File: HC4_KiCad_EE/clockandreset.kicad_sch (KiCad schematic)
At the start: 18 parts, among them IC15 74HC14, SW2 SW_Push, SW3 SW_Push, SW4 FreqSel, SW5 SW_SPDT

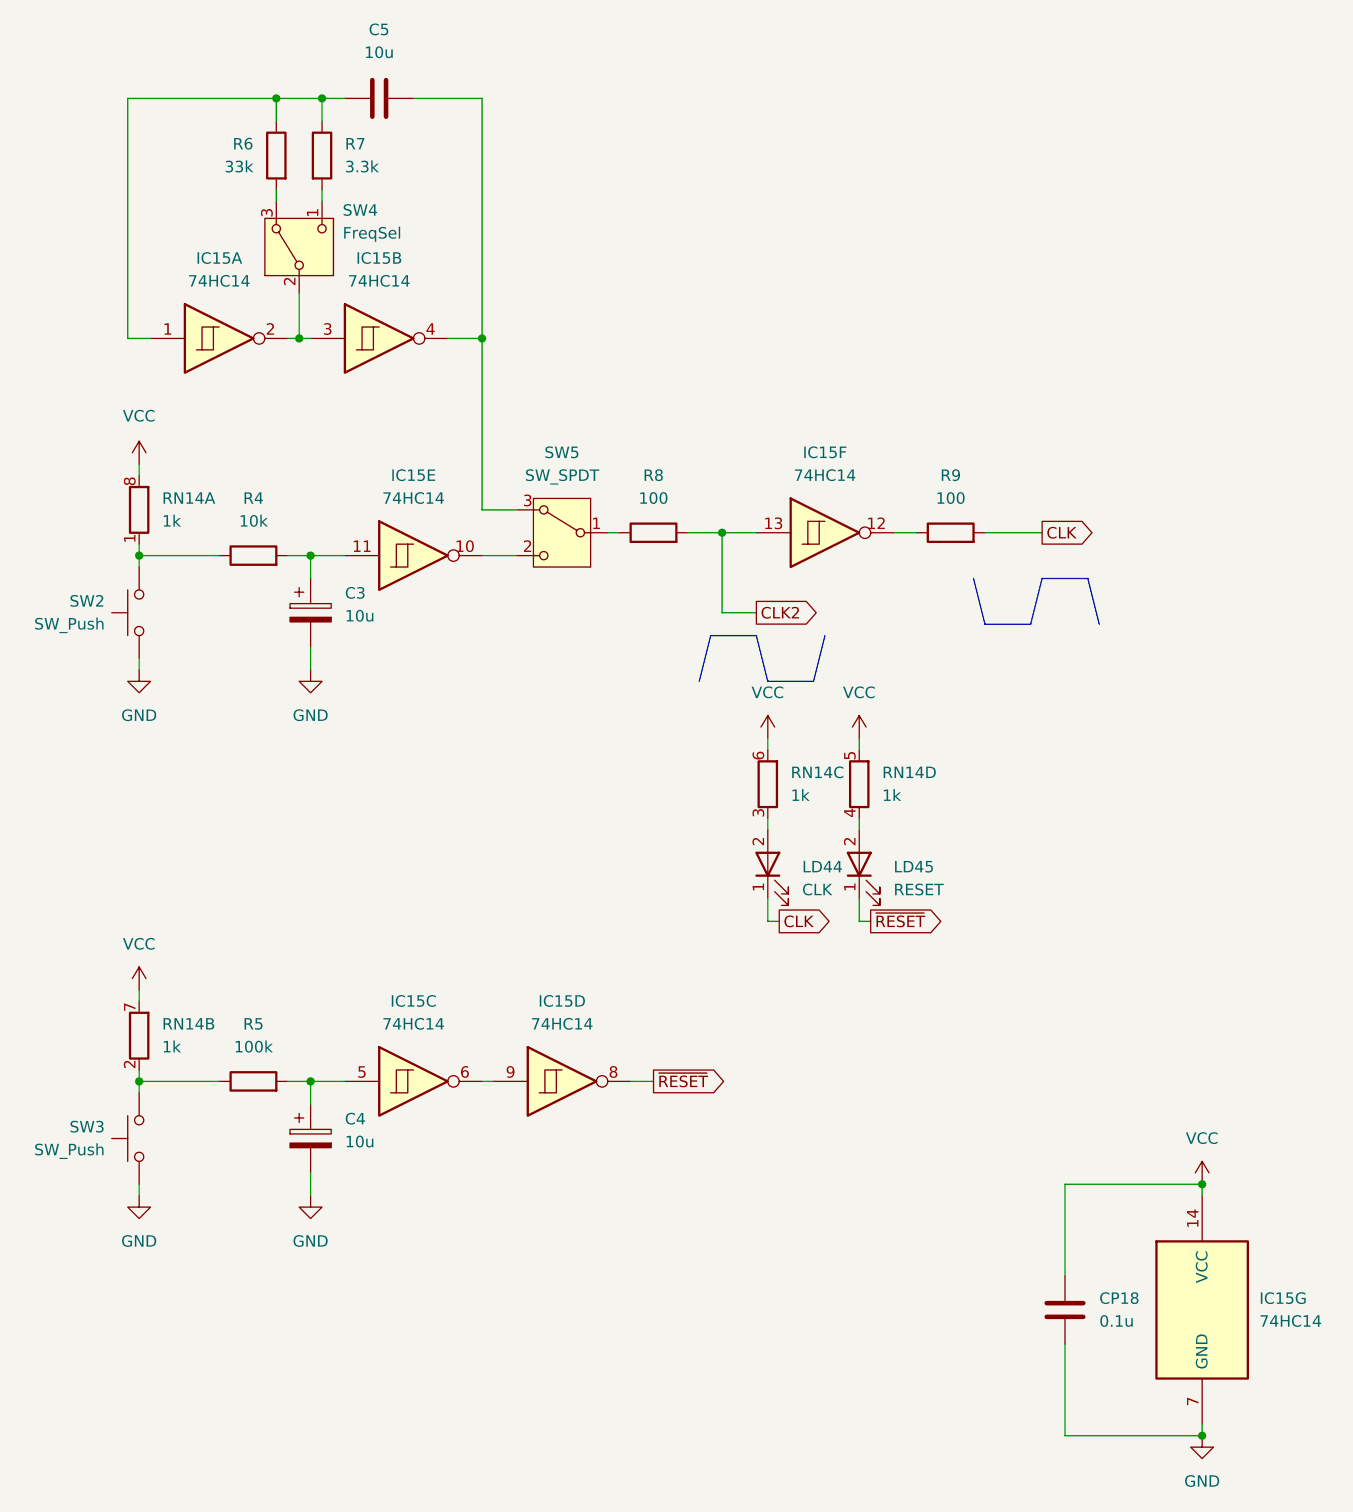
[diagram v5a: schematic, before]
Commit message: 配線進捗、7474を使った変な回路
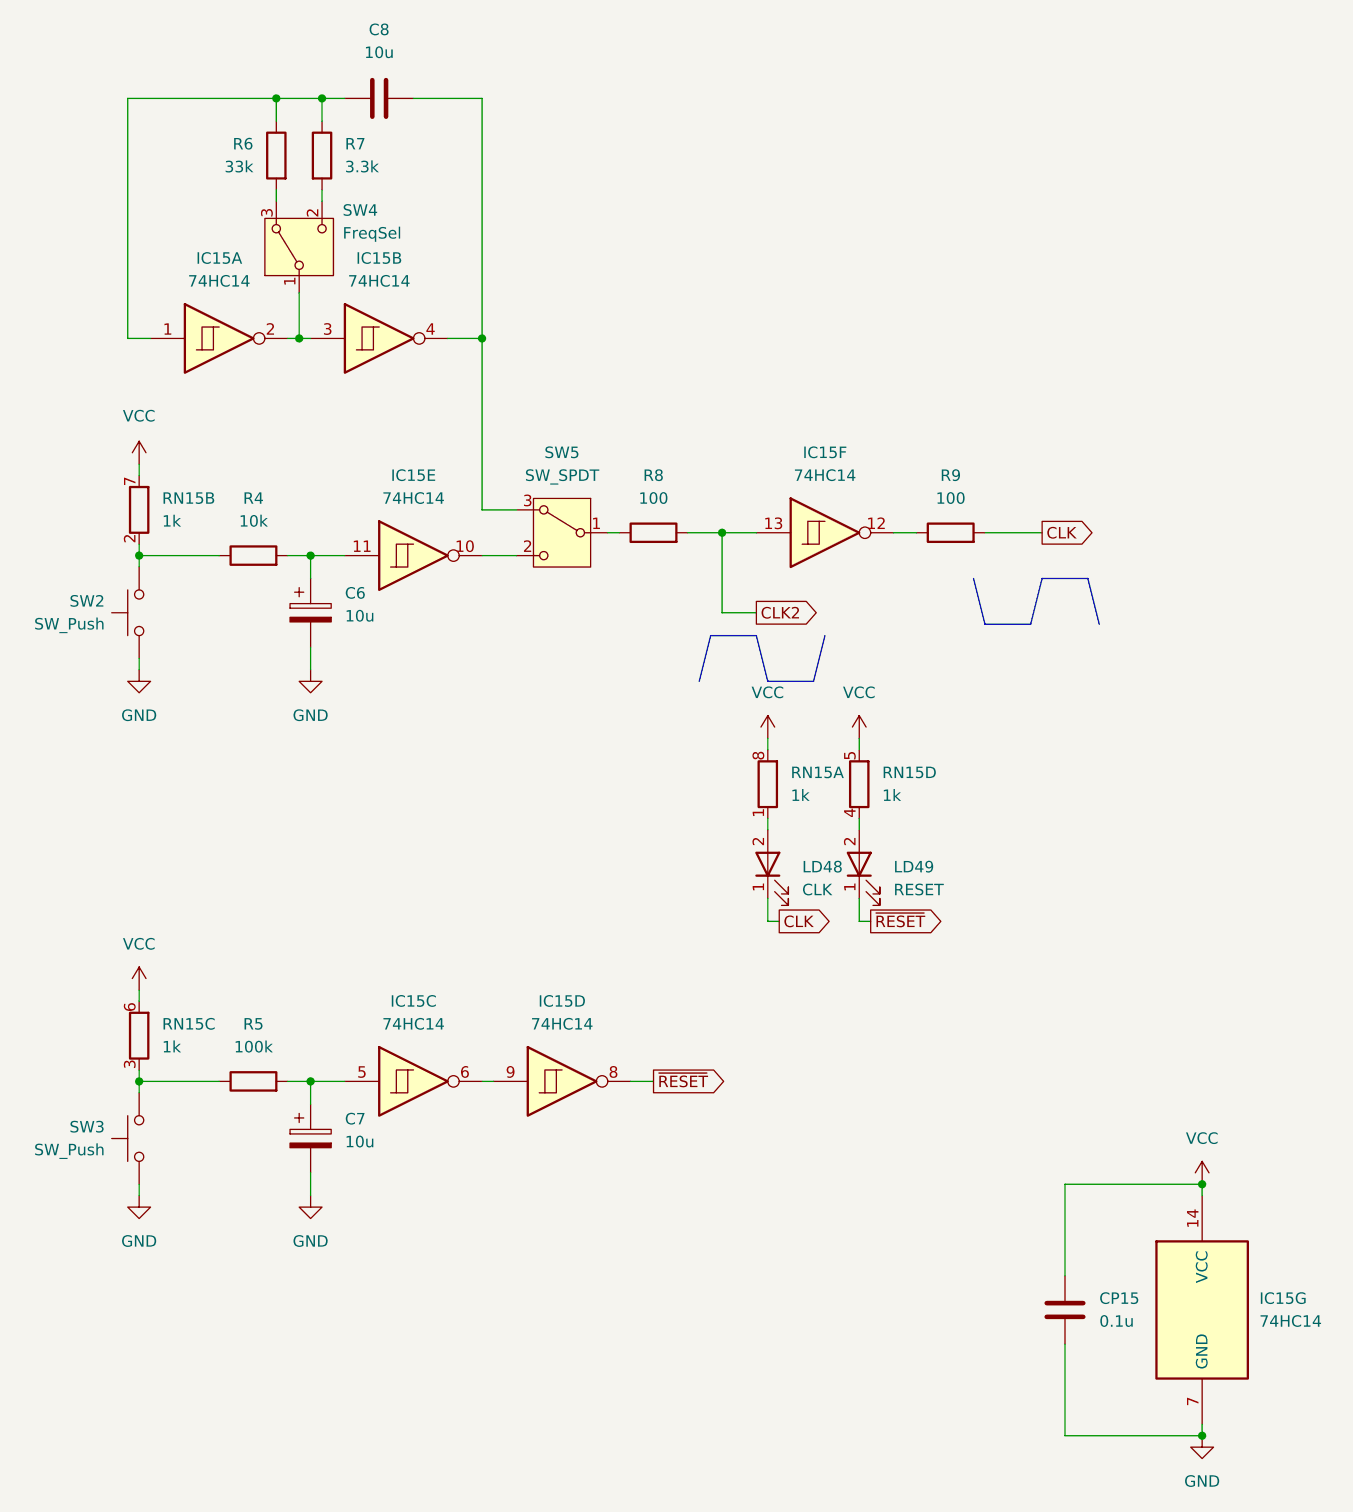
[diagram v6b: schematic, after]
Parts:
- SW4: symbol Switch:SW_SPDT_321 -> Switch:SW_SPDT_312
- renumbered C3 to C6, C4 to C7, C5 to C8, CP18 to CP15, LD44 to LD48, LD45 to LD49, RN14 to RN15
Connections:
- net at R4.1, SW2.2: now also RN15.2 (R2.1); no longer RN15.1 (R1.1)
- net at R5.1, SW3.2: now also RN15.3 (R3.1); no longer RN15.2 (R2.1)
- net at SW4.1 (B): now also IC15.2, IC15.3; no longer R7.2
- net at LD48.2: now also RN15.1 (R1.1); no longer RN15.3 (R3.1)
- new net: R7.2, SW4.2 (C)
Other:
- moved on the sheet: RN15A, RN15B, RN15C
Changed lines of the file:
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@@
 		(dnp no)
 		(fields_autoplaced yes)
-		(property "Reference" "RN14"
+		(property "Reference" "RN15"
 			(at 120.65 116.8399 0)
 			(effects
@@
 			(project ""
 				(path "/33731ded-38c0-4297-bdd8-92b082f46ff8/3d67359d-c55c-4207-8a6b-ff7c83e276f6"
-					(reference "RN14")
+					(reference "RN15")
 					(unit 4)
 				)
@@
 	(symbol
 		(lib_id "Device:R_Pack04_Split")
-		(at 38.1 146.05 0)
+		(at 38.1 87.63 0)
 		(unit 2)
 		(exclude_from_sim no)
@@
 		(dnp no)
 		(fields_autoplaced yes)
-		(property "Reference" "RN14"
-			(at 40.64 144.7799 0)
+		(property "Reference" "RN15"
+			(at 40.64 86.3599 0)
 			(effects
 				(font
@@
 		)
 		(property "Value" "1k"
-			(at 40.64 147.3199 0)
+			(at 40.64 88.8999 0)
 			(effects
 				(font
@@
 		)
 		(property "Footprint" "Resistor_SMD:R_Array_Convex_4x0603"
-			(at 36.068 146.05 90)
+			(at 36.068 87.63 90)
 			(effects
 				(font
@@
 		)
 		(property "Datasheet" "~"
-			(at 38.1 146.05 0)
+			(at 38.1 87.63 0)
 			(effects
 				(font
@@
 		)
 		(property "Description" "4 resistor network, parallel topology, split"
-			(at 38.1 146.05 0)
+			(at 38.1 87.63 0)
 			(effects
 				(font
@@
 			(project ""
 				(path "/33731ded-38c0-4297-bdd8-92b082f46ff8/3d67359d-c55c-4207-8a6b-ff7c83e276f6"
-					(reference "RN14")
+					(reference "RN15")
 					(unit 2)
 				)
@@
 		(dnp no)
 		(fields_autoplaced yes)
-		(property "Reference" "#PWR073"
+		(property "Reference" "#PWR072"
 			(at 118.11 116.84 0)
 			(effects
@@
 			(project ""
 				(path "/33731ded-38c0-4297-bdd8-92b082f46ff8/3d67359d-c55c-4207-8a6b-ff7c83e276f6"
-					(reference "#PWR073")
+					(reference "#PWR072")
 					(unit 1)
 				)
@@
 		(dnp no)
 		(fields_autoplaced yes)
-		(property "Reference" "C5"
+		(property "Reference" "C8"
 			(at 64.77 34.29 90)
 			(effects
@@
 			(project ""
 				(path "/33731ded-38c0-4297-bdd8-92b082f46ff8/3d67359d-c55c-4207-8a6b-ff7c83e276f6"
-					(reference "C5")
+					(reference "C8")
 					(unit 1)
 				)
@@
 		(dnp no)
 		(fields_autoplaced yes)
-		(property "Reference" "#PWR067"
+		(property "Reference" "#PWR066"
 			(at 38.1 111.76 0)
 			(effects
@@
 			(project "HC4_KiCad"
 				(path "/33731ded-38c0-4297-bdd8-92b082f46ff8/3d67359d-c55c-4207-8a6b-ff7c83e276f6"
-					(reference "#PWR067")
-					(unit 1)
-				)
-			)
-		)
-	)
-	(symbol
-		(lib_id "Switch:SW_SPDT_321")
+					(reference "#PWR066")
+					(unit 1)
+				)
+			)
+		)
+	)
+	(symbol
+		(lib_id "Switch:SW_SPDT_312")
 		(at 55.88 58.42 90)
 		(unit 1)
@@
 		(dnp no)
 		(fields_autoplaced yes)
-		(property "Reference" "C3"
+		(property "Reference" "C6"
 			(at 60.96 96.9009 0)
 			(effects
@@
 			(project ""
 				(path "/33731ded-38c0-4297-bdd8-92b082f46ff8/3d67359d-c55c-4207-8a6b-ff7c83e276f6"
-					(reference "C3")
+					(reference "C6")
 					(unit 1)
 				)
@@
 		(dnp no)
 		(fields_autoplaced yes)
-		(property "Reference" "#PWR070"
+		(property "Reference" "#PWR069"
 			(at 57.15 111.76 0)
 			(effects
@@
 			(project ""
 				(path "/33731ded-38c0-4297-bdd8-92b082f46ff8/3d67359d-c55c-4207-8a6b-ff7c83e276f6"
-					(reference "#PWR070")
+					(reference "#PWR069")
 					(unit 1)
 				)
@@
 		(dnp no)
 		(fields_autoplaced yes)
-		(property "Reference" "CP18"
+		(property "Reference" "CP15"
 			(at 144.78 175.2599 0)
 			(effects
@@
 			(project ""
 				(path "/33731ded-38c0-4297-bdd8-92b082f46ff8/3d67359d-c55c-4207-8a6b-ff7c83e276f6"
-					(reference "CP18")
+					(reference "CP15")
 					(unit 1)
 				)
@@
 		(dnp no)
 		(fields_autoplaced yes)
-		(property "Reference" "#PWR071"
+		(property "Reference" "#PWR070"
 			(at 57.15 170.18 0)
 			(effects
@@
 			(project "HC4_KiCad"
 				(path "/33731ded-38c0-4297-bdd8-92b082f46ff8/3d67359d-c55c-4207-8a6b-ff7c83e276f6"
-					(reference "#PWR071")
+					(reference "#PWR070")
 					(unit 1)
 				)
@@
 		(dnp no)
 		(fields_autoplaced yes)
-		(property "Reference" "LD44"
+		(property "Reference" "LD48"
 			(at 111.76 127.3174 90)
 			(effects
@@
 			(project ""
 				(path "/33731ded-38c0-4297-bdd8-92b082f46ff8/3d67359d-c55c-4207-8a6b-ff7c83e276f6"
-					(reference "LD44")
+					(reference "LD48")
 					(unit 1)
 				)
@@
 		(dnp no)
 		(fields_autoplaced yes)
-		(property "Reference" "C4"
+		(property "Reference" "C7"
 			(at 60.96 155.3209 0)
 			(effects
@@
 			(project ""
 				(path "/33731ded-38c0-4297-bdd8-92b082f46ff8/3d67359d-c55c-4207-8a6b-ff7c83e276f6"
-					(reference "C4")
+					(reference "C7")
 					(unit 1)
 				)
@@
 	(symbol
 		(lib_id "Device:R_Pack04_Split")
-		(at 38.1 87.63 0)
-		(unit 1)
-		(exclude_from_sim no)
-		(in_bom yes)
-		(on_board yes)
-		(dnp no)
-		(fields_autoplaced yes)
-		(property "Reference" "RN14"
-			(at 40.64 86.3599 0)
+		(at 107.95 118.11 0)
+		(unit 1)
+		(exclude_from_sim no)
+		(in_bom yes)
+		(on_board yes)
+		(dnp no)
+		(fields_autoplaced yes)
+		(property "Reference" "RN15"
+			(at 110.49 116.8399 0)
 			(effects
 				(font
@@
 		)
 		(property "Value" "1k"
-			(at 40.64 88.8999 0)
+			(at 110.49 119.3799 0)
 			(effects
 				(font
@@
 		)
 		(property "Footprint" "Resistor_SMD:R_Array_Convex_4x0603"
-			(at 36.068 87.63 90)
+			(at 105.918 118.11 90)
 			(effects
 				(font
@@
 		)
 		(property "Datasheet" "~"
-			(at 38.1 87.63 0)
+			(at 107.95 118.11 0)
 			(effects
 				(font
@@
 		)
 		(property "Description" "4 resistor network, parallel topology, split"
-			(at 38.1 87.63 0)
+			(at 107.95 118.11 0)
 			(effects
 				(font
@@
 			(project ""
 				(path "/33731ded-38c0-4297-bdd8-92b082f46ff8/3d67359d-c55c-4207-8a6b-ff7c83e276f6"
-					(reference "RN14")
+					(reference "RN15")
 					(unit 1)
 				)
@@
 		(dnp no)
 		(fields_autoplaced yes)
-		(property "Reference" "#PWR069"
+		(property "Reference" "#PWR068"
 			(at 38.1 170.18 0)
 			(effects
@@
 			(project ""
 				(path "/33731ded-38c0-4297-bdd8-92b082f46ff8/3d67359d-c55c-4207-8a6b-ff7c83e276f6"
-					(reference "#PWR069")
+					(reference "#PWR068")
 					(unit 1)
 				)
@@
 		(dnp no)
 		(fields_autoplaced yes)
-		(property "Reference" "#PWR072"
+		(property "Reference" "#PWR071"
 			(at 107.95 116.84 0)
 			(effects
@@
 			(project "HC4_KiCad"
 				(path "/33731ded-38c0-4297-bdd8-92b082f46ff8/3d67359d-c55c-4207-8a6b-ff7c83e276f6"
-					(reference "#PWR072")
+					(reference "#PWR071")
 					(unit 1)
 				)
@@
 		(dnp no)
 		(fields_autoplaced yes)
-		(property "Reference" "LD45"
+		(property "Reference" "LD49"
 			(at 121.92 127.3174 90)
 			(effects
@@
 			(project "HC4_KiCad"
 				(path "/33731ded-38c0-4297-bdd8-92b082f46ff8/3d67359d-c55c-4207-8a6b-ff7c83e276f6"
-					(reference "LD45")
+					(reference "LD49")
 					(unit 1)
 				)
@@
 		(dnp no)
 		(fields_autoplaced yes)
-		(property "Reference" "#PWR068"
+		(property "Reference" "#PWR067"
 			(at 38.1 144.78 0)
 			(effects
@@
 			(project ""
 				(path "/33731ded-38c0-4297-bdd8-92b082f46ff8/3d67359d-c55c-4207-8a6b-ff7c83e276f6"
-					(reference "#PWR068")
+					(reference "#PWR067")
 					(unit 1)
 				)
@@
 	(symbol
 		(lib_id "Device:R_Pack04_Split")
-		(at 107.95 118.11 0)
+		(at 38.1 146.05 0)
 		(unit 3)
 		(exclude_from_sim no)
@@
 		(dnp no)
 		(fields_autoplaced yes)
-		(property "Reference" "RN14"
-			(at 110.49 116.8399 0)
+		(property "Reference" "RN15"
+			(at 40.64 144.7799 0)
 			(effects
 				(font
@@
 		)
 		(property "Value" "1k"
-			(at 110.49 119.3799 0)
+			(at 40.64 147.3199 0)
 			(effects
 				(font
@@
 		)
 		(property "Footprint" "Resistor_SMD:R_Array_Convex_4x0603"
-			(at 105.918 118.11 90)
+			(at 36.068 146.05 90)
 			(effects
 				(font
@@
 		)
 		(property "Datasheet" "~"
-			(at 107.95 118.11 0)
+			(at 38.1 146.05 0)
 			(effects
 				(font
@@
 		)
 		(property "Description" "4 resistor network, parallel topology, split"
-			(at 107.95 118.11 0)
+			(at 38.1 146.05 0)
 			(effects
 				(font
@@
 			(project ""
 				(path "/33731ded-38c0-4297-bdd8-92b082f46ff8/3d67359d-c55c-4207-8a6b-ff7c83e276f6"
-					(reference "RN14")
+					(reference "RN15")
 					(unit 3)
 				)
@@
 		(on_board yes)
 		(dnp no)
-		(property "Reference" "#PWR066"
+		(property "Reference" "#PWR065"
 			(at 38.1 86.36 0)
 			(effects
@@
 			(project "HC4_KiCad"
 				(path "/33731ded-38c0-4297-bdd8-92b082f46ff8/3d67359d-c55c-4207-8a6b-ff7c83e276f6"
-					(reference "#PWR066")
+					(reference "#PWR065")
 					(unit 1)
 				)
@@
 		(dnp no)
 		(fields_autoplaced yes)
-		(property "Reference" "#PWR075"
+		(property "Reference" "#PWR074"
 			(at 156.21 196.85 0)
 			(effects
@@
 			(project ""
 				(path "/33731ded-38c0-4297-bdd8-92b082f46ff8/3d67359d-c55c-4207-8a6b-ff7c83e276f6"
-					(reference "#PWR075")
+					(reference "#PWR074")
 					(unit 1)
 				)
@@
 		(dnp no)
 		(fields_autoplaced yes)
-		(property "Reference" "#PWR074"
+		(property "Reference" "#PWR073"
 			(at 156.21 166.37 0)
 			(effects
@@
 			(project ""
 				(path "/33731ded-38c0-4297-bdd8-92b082f46ff8/3d67359d-c55c-4207-8a6b-ff7c83e276f6"
-					(reference "#PWR074")
-					(unit 1)
-				)
+					(reference "#PWR073")
+					(unit 1)
+				)

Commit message: もち
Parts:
- renumbered LD48 to LD46, LD49 to LD47
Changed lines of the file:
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@@
 		(dnp no)
 		(fields_autoplaced yes)
-		(property "Reference" "#PWR072"
+		(property "Reference" "#PWR074"
 			(at 118.11 116.84 0)
 			(effects
@@
 			(project ""
 				(path "/33731ded-38c0-4297-bdd8-92b082f46ff8/3d67359d-c55c-4207-8a6b-ff7c83e276f6"
-					(reference "#PWR072")
+					(reference "#PWR074")
 					(unit 1)
 				)
@@
 		(dnp no)
 		(fields_autoplaced yes)
-		(property "Reference" "#PWR066"
+		(property "Reference" "#PWR068"
 			(at 38.1 111.76 0)
 			(effects
@@
 			(project "HC4_KiCad"
 				(path "/33731ded-38c0-4297-bdd8-92b082f46ff8/3d67359d-c55c-4207-8a6b-ff7c83e276f6"
-					(reference "#PWR066")
+					(reference "#PWR068")
 					(unit 1)
 				)
@@
 		(dnp no)
 		(fields_autoplaced yes)
-		(property "Reference" "#PWR069"
+		(property "Reference" "#PWR071"
 			(at 57.15 111.76 0)
 			(effects
@@
 			(project ""
 				(path "/33731ded-38c0-4297-bdd8-92b082f46ff8/3d67359d-c55c-4207-8a6b-ff7c83e276f6"
-					(reference "#PWR069")
+					(reference "#PWR071")
 					(unit 1)
 				)
@@
 		(dnp no)
 		(fields_autoplaced yes)
-		(property "Reference" "#PWR070"
+		(property "Reference" "#PWR072"
 			(at 57.15 170.18 0)
 			(effects
@@
 			(project "HC4_KiCad"
 				(path "/33731ded-38c0-4297-bdd8-92b082f46ff8/3d67359d-c55c-4207-8a6b-ff7c83e276f6"
-					(reference "#PWR070")
+					(reference "#PWR072")
 					(unit 1)
 				)
@@
 		(dnp no)
 		(fields_autoplaced yes)
-		(property "Reference" "LD48"
+		(property "Reference" "LD46"
 			(at 111.76 127.3174 90)
 			(effects
@@
 			(project ""
 				(path "/33731ded-38c0-4297-bdd8-92b082f46ff8/3d67359d-c55c-4207-8a6b-ff7c83e276f6"
-					(reference "LD48")
+					(reference "LD46")
 					(unit 1)
 				)
@@
 		(dnp no)
 		(fields_autoplaced yes)
-		(property "Reference" "#PWR068"
+		(property "Reference" "#PWR070"
 			(at 38.1 170.18 0)
 			(effects
@@
 			(project ""
 				(path "/33731ded-38c0-4297-bdd8-92b082f46ff8/3d67359d-c55c-4207-8a6b-ff7c83e276f6"
-					(reference "#PWR068")
+					(reference "#PWR070")
 					(unit 1)
 				)
@@
 		(dnp no)
 		(fields_autoplaced yes)
-		(property "Reference" "#PWR071"
+		(property "Reference" "#PWR073"
 			(at 107.95 116.84 0)
 			(effects
@@
 			(project "HC4_KiCad"
 				(path "/33731ded-38c0-4297-bdd8-92b082f46ff8/3d67359d-c55c-4207-8a6b-ff7c83e276f6"
-					(reference "#PWR071")
+					(reference "#PWR073")
 					(unit 1)
 				)
@@
 		(dnp no)
 		(fields_autoplaced yes)
-		(property "Reference" "LD49"
+		(property "Reference" "LD47"
 			(at 121.92 127.3174 90)
 			(effects
@@
 			(project "HC4_KiCad"
 				(path "/33731ded-38c0-4297-bdd8-92b082f46ff8/3d67359d-c55c-4207-8a6b-ff7c83e276f6"
-					(reference "LD49")
+					(reference "LD47")
 					(unit 1)
 				)
@@
 		(dnp no)
 		(fields_autoplaced yes)
-		(property "Reference" "#PWR067"
+		(property "Reference" "#PWR069"
 			(at 38.1 144.78 0)
 			(effects
@@
 			(project ""
 				(path "/33731ded-38c0-4297-bdd8-92b082f46ff8/3d67359d-c55c-4207-8a6b-ff7c83e276f6"
-					(reference "#PWR067")
+					(reference "#PWR069")
 					(unit 1)
 				)
@@
 		(on_board yes)
 		(dnp no)
-		(property "Reference" "#PWR065"
+		(property "Reference" "#PWR067"
 			(at 38.1 86.36 0)
 			(effects
@@
 			(project "HC4_KiCad"
 				(path "/33731ded-38c0-4297-bdd8-92b082f46ff8/3d67359d-c55c-4207-8a6b-ff7c83e276f6"
-					(reference "#PWR065")
+					(reference "#PWR067")
 					(unit 1)
 				)
@@
 		(dnp no)
 		(fields_autoplaced yes)
-		(property "Reference" "#PWR074"
+		(property "Reference" "#PWR076"
 			(at 156.21 196.85 0)
 			(effects
@@
 			(project ""
 				(path "/33731ded-38c0-4297-bdd8-92b082f46ff8/3d67359d-c55c-4207-8a6b-ff7c83e276f6"
-					(reference "#PWR074")
+					(reference "#PWR076")
 					(unit 1)
 				)
@@
 		(dnp no)
 		(fields_autoplaced yes)
-		(property "Reference" "#PWR073"
+		(property "Reference" "#PWR075"
 			(at 156.21 166.37 0)
 			(effects
@@
 			(project ""
 				(path "/33731ded-38c0-4297-bdd8-92b082f46ff8/3d67359d-c55c-4207-8a6b-ff7c83e276f6"
-					(reference "#PWR073")
-					(unit 1)
-				)
+					(reference "#PWR075")
+					(unit 1)
+				)
